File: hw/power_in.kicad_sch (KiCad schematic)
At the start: 23 parts, among them J1 24V_IN, U1 LMR38020SDDAR

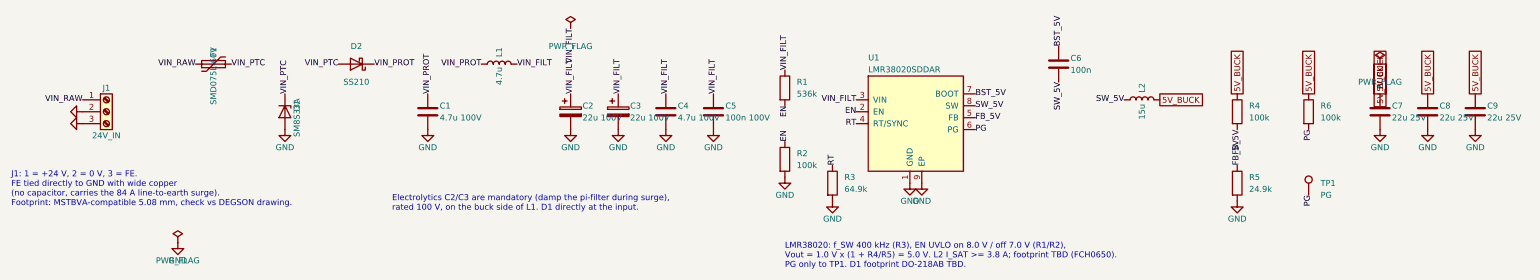
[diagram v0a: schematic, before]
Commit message: hw: draw schematic with wires instead of net labels
Connections inside a sheet are now wires; global labels remain only for
nets that cross sheets, GND stays on power symbols. Pico pins 9-20 are
fanned out so the 33R series resistors fit in one column, and the
SX1302_RESET pull-down moves to the LoRa sheet. Netlist unchanged, ERC
clean. Project file now carries KiCad's default settings.

Co-Authored-By: Claude Opus 5.5 <noreply@anthropic.com>
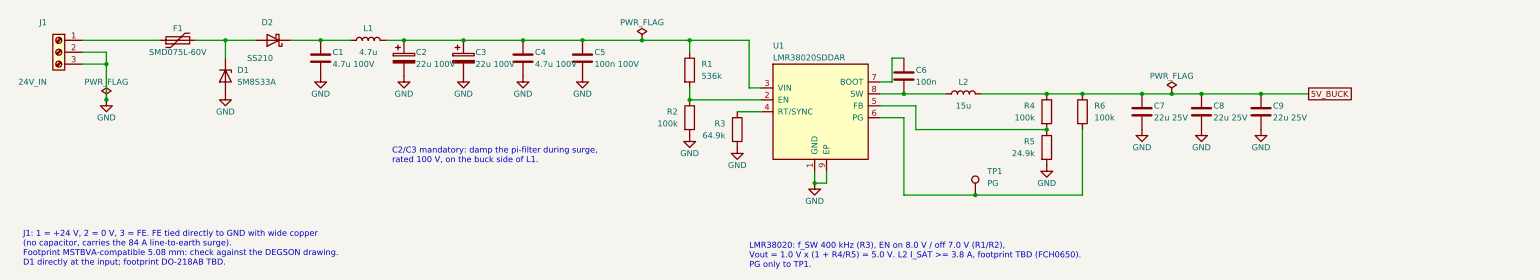
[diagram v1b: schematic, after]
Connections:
- net BST_5V: no longer names the net of C6.1, U1.7 (BOOT)
- net EN: no longer names the net of R1.2, R2.1, U1.2 (EN)
- net FB_5V: no longer names the net of R4.2, R5.1, U1.5 (FB)
- net PG: no longer names the net of R6.2, TP1.1, U1.6 (PG)
- net RT: no longer names the net of R3.1, U1.4 (RT/SYNC)
- net SW_5V: no longer names the net of C6.2, L2.1, U1.8 (SW)
- net VIN_FILT: no longer names the net of C2.1, C3.1, C4.1, C5.1, L1.2, R1.1, U1.3 (VIN)
- net VIN_PROT: no longer names the net of C1.1, D2.1 (K), L1.1
- net VIN_PTC: no longer names the net of D1.1 (K), D2.2 (A), F1.2
- net VIN_RAW: no longer names the net of F1.1, J1.1 (Pin_1)
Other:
- note added: "C2/C3 mandatory: damp the pi-filter during surge, rated 100 V, on the buck side of L1."
- note added: "J1: 1 = +24 V, 2 = 0 V, 3 = FE. FE tied directly to GND with wide copper (no capacitor, carries the 84 A line-to-earth surge). Footprint MSTBVA-compatible 5.08 mm: check against the DEGSON drawing. D1 directly at the input; footprint DO-218AB TBD."
- note added: "LMR38020: f_SW 400 kHz (R3), EN on 8.0 V / off 7.0 V (R1/R2), Vout = 1.0 V x (1 + R4/R5) = 5.0 V. L2 I_SAT >= 3.8 A, footprint TBD (FCH0650). PG only to TP1."
- note removed: "Electrolytics C2/C3 are mandatory (damp the pi-filter during surge), rated 100 V, on the buck side of L1. D1 directly at the input."
- note removed: "J1: 1 = +24 V, 2 = 0 V, 3 = FE. FE tied directly to GND with wide copper (no capacitor, carries the 84 A line-to-earth surge). Footprint: MSTBVA-compatible 5.08 mm, check vs DEGSON drawing."
- note removed: "LMR38020: f_SW 400 kHz (R3), EN UVLO on 8.0 V / off 7.0 V (R1/R2), Vout = 1.0 V x (1 + R4/R5) = 5.0 V. L2 I_SAT >= 3.8 A; footprint TBD (FCH0650). PG only to TP1. D1 footprint DO-218AB TBD."
- moved on the sheet: C1, C2, C3, C4, C5, C6, C7, C8, C9, D1, D2, F1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
